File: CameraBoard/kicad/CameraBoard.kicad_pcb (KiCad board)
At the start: 2 copper layers, 101.6 x 76.2 mm, 56 parts, among them Q1 SUD08P06-155L, Q2 SUD08P06-155L, Q3 SUD08P06-155L, U1 LM2678SD-12/NOPB, U1 MP2659GQ-0000-Z

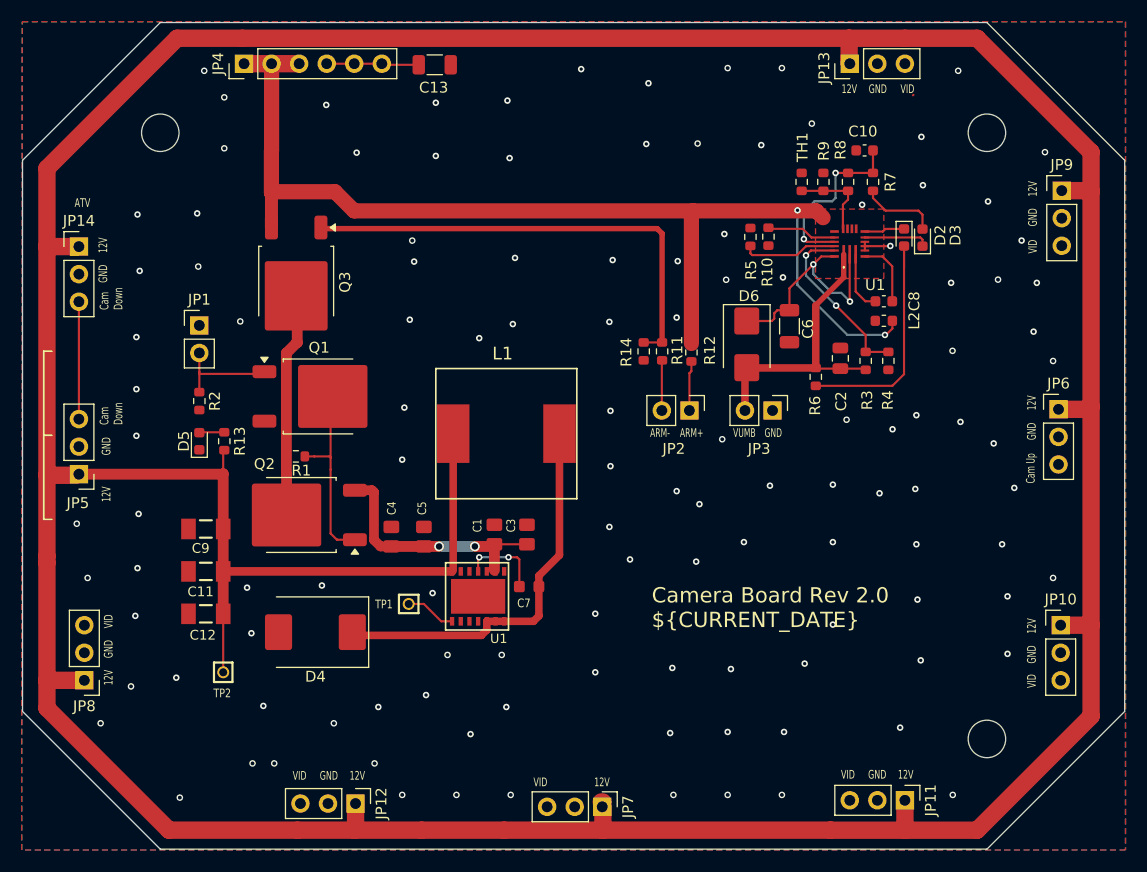
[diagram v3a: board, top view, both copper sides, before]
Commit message: Small update to PCB
Fixed some unsnapped traces
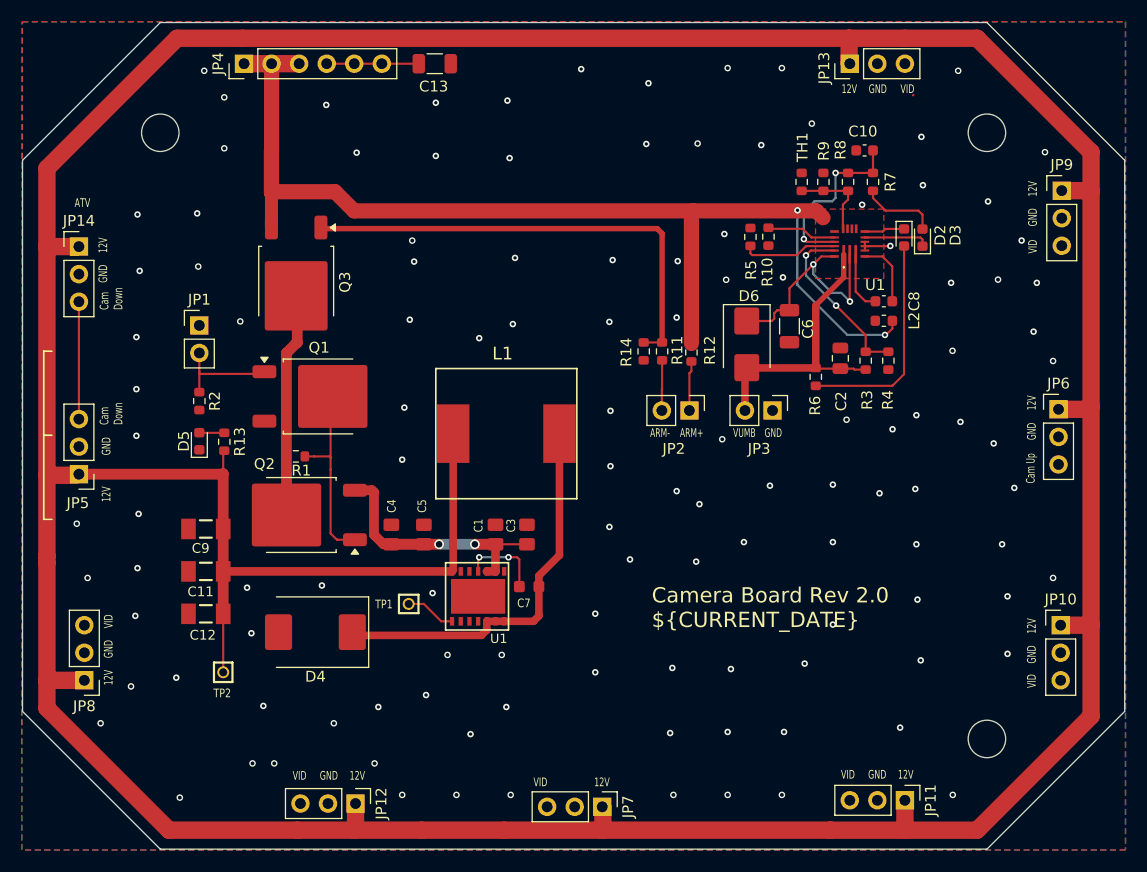
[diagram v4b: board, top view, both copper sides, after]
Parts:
- moved C4 0.20 mm to (131.7, 114.1)
- moved C5 0.20 mm to (134.7, 114.1)
- moved C1 0.10 mm to (141.3, 114.1)
- moved C13 0.10 mm to (135.7, 70.7)
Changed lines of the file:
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@@
 	(footprint "CameraBoard:.0805-B-NOSILK"
 		(layer "F.Cu")
-		(at 141.2 114.1 90)
+		(at 141.3 114.1 90)
 		(descr "0805 (metric 2012) normal 'IPC-B' without silkscreen\nIn house package for nominal spacing based on IPC-7351B. This package is identical to 0805-B, but has its tPlace silkscreen layer removed.")
 		(property "Reference" "C1"
@@
 	(footprint "CameraBoard:.0805-B-NOSILK"
 		(layer "F.Cu")
-		(at 131.7 114.3 90)
+		(at 131.7 114.1 90)
 		(descr "0805 (metric 2012) normal 'IPC-B' without silkscreen\nIn house package for nominal spacing based on IPC-7351B. This package is identical to 0805-B, but has its tPlace silkscreen layer removed.")
 		(property "Reference" "C4"
@@
 	(footprint "CameraBoard:.0805-B-NOSILK"
 		(layer "F.Cu")
-		(at 134.7 114.3 90)
+		(at 134.7 114.1 90)
 		(descr "0805 (metric 2012) normal 'IPC-B' without silkscreen\nIn house package for nominal spacing based on IPC-7351B. This package is identical to 0805-B, but has its tPlace silkscreen layer removed.")
 		(property "Reference" "C5"
@@
 	(footprint "Capacitor_SMD:C_1206_3216Metric"
 		(layer "F.Cu")
-		(at 135.7 70.8)
+		(at 135.7 70.7)
 		(descr "Capacitor SMD 1206 (3216 Metric), square (rectangular) end terminal, IPC-7351 nominal, (Body size source: IPC-SM-782 page 76, https://www.pcb-3d.com/wordpress/wp-content/uploads/ipc-sm-782a_amendment_1_and_2.pdf)")
 		(tags "capacitor")
@@
 	(footprint "Resistor_SMD:R_0603_1608Metric"
 		(layer "F.Cu")
-		(at 116.3 105.5 -90)
+		(at 116.3 105.55 -90)
 		(descr "Resistor SMD 0603 (1608 Metric), square (rectangular) end terminal, IPC-7351 nominal, (Body size source: IPC-SM-782 page 72, https://www.pcb-3d.com/wordpress/wp-content/uploads/ipc-sm-782a_amendment_1_and_2.pdf)")
 		(tags "resistor")
@@
 	(footprint "Resistor_SMD:R_0603_1608Metric"
 		(layer "F.Cu")
-		(at 177.515 98.09375 90)
+		(at 177.515 98.075 90)
 		(descr "Resistor SMD 0603 (1608 Metric), square (rectangular) end terminal, IPC-7351 nominal, (Body size source: IPC-SM-782 page 72, https://www.pcb-3d.com/wordpress/wp-content/uploads/ipc-sm-782a_amendment_1_and_2.pdf)")
 		(tags "resistor")
@@
 	(footprint "Resistor_SMD:R_0603_1608Metric"
 		(layer "F.Cu")
-		(at 175.425 98.09375 -90)
+		(at 175.425 98.075 -90)
 		(descr "Resistor SMD 0603 (1608 Metric), square (rectangular) end terminal, IPC-7351 nominal, (Body size source: IPC-SM-782 page 72, https://www.pcb-3d.com/wordpress/wp-content/uploads/ipc-sm-782a_amendment_1_and_2.pdf)")
 		(tags "resistor")
@@
 	)
 	(gr_line
-		(start 128.325 96.1475)
-		(end 128.325 122.8975)
-		(stroke
-			(width 0.001)
-			(type solid)
-		)
-		(layer "Cmts.User")
-	)
-	(gr_line
 		(start 97.7011 79.6036)
 		(end 97.7011 130.4036)
@@
 	)
 	(segment
-		(start 151.2011 141.3536)
-		(end 151.2011 139.2611)
+		(start 151.2011 139.2611)
+		(end 151.14 139.2)
 		(width 1.6)
 		(layer "F.Cu")
@@
 	)
 	(segment
-		(start 151.2011 138.7536)
-		(end 151.0411 138.7536)
-		(width 1.6)
-		(layer "F.Cu")
-		(net "+12V")
-	)
-	(segment
 		(start 116.2 108.5)
 		(end 116.2 106.425)
@@
 	)
 	(segment
-		(start 102.7 108.64)
-		(end 99.9911 108.64)
+		(start 151.2011 141.3536)
+		(end 151.2011 139.2611)
 		(width 1.6)
 		(layer "F.Cu")
@@
 	)
 	(segment
-		(start 128.3 141.3536)
-		(end 123.0411 141.3536)
+		(start 102.7 108.64)
+		(end 99.9911 108.64)
 		(width 1.6)
 		(layer "F.Cu")
@@
 	)
 	(segment
-		(start 151.2011 139.2611)
-		(end 151.14 139.2)
+		(start 128.3 141.3536)
+		(end 123.0411 141.3536)
 		(width 1.6)
 		(layer "F.Cu")
@@
 		(net "GND")
 	)
-	(segment
-		(start 114.0875 106.2)
-		(end 114 106.2875)
-		(width 0.2)
-		(layer "F.Cu")
-		(net "GND")
-	)
 	(via
 		(at 167.7011 138.1036)
@@
 	)
 	(segment
+		(start 174.4 98.9)
+		(end 175.425 98.9)
+		(width 0.2)
+		(layer "F.Cu")
+		(net "/VUMB")
+	)
+	(segment
 		(start 164.2975 102.66875)
 		(end 164.2975 98.88375)
@@
 	)
 	(segment
-		(start 175.425 98.91875)
-		(end 175.315 98.80875)
+		(start 173.09 98.80875)
+		(end 174.30875 98.80875)
 		(width 0.2)
 		(layer "F.Cu")
@@
 	)
 	(segment
-		(start 175.315 98.80875)
-		(end 173.09 98.80875)
+		(start 174.30875 98.80875)
+		(end 174.4 98.9)
 		(width 0.2)
 		(layer "F.Cu")
@@
 	)
 	(segment
-		(start 141.2 115)
-		(end 141.2 117.4)
-		(width 1)
-		(layer "F.Cu")
-		(net "Net-(Q2-S)")
-	)
-	(segment
-		(start 130.1 114.6)
-		(end 130.1 110.2)
+		(start 130.1 110.2)
+		(end 130.1 114.124999)
 		(width 0.9)
 		(layer "F.Cu")
@@
 	)
 	(segment
-		(start 139.4 115.2)
-		(end 141 115.2)
-		(width 1)
+		(start 141.3 117.5)
+		(end 140.5 117.5)
+		(width 0.8)
 		(layer "F.Cu")
 		(net "Net-(Q2-S)")
 	)
 	(segment
-		(start 140.6 117.4)
-		(end 140.5 117.5)
-		(width 0.2)
+		(start 134.7 115)
+		(end 136.1 115)
+		(width 1)
 		(layer "F.Cu")
 		(net "Net-(Q2-S)")
 	)
 	(segment
-		(start 134.7 115.2)
-		(end 136.1 115.2)
-		(width 1)
+		(start 141.3 115)
+		(end 141.3 117.5)
+		(width 0.8)
 		(layer "F.Cu")
 		(net "Net-(Q2-S)")
 	)
 	(segment
-		(start 131.7 115.2)
-		(end 130.7 115.2)
-		(width 0.9)
+		(start 139.4 115)
+		(end 141.2 115)
+		(width 1)
 		(layer "F.Cu")
 		(net "Net-(Q2-S)")
@@
 	)
 	(segment
-		(start 131.7 115.2)
-		(end 134.7 115.2)
+		(start 131.7 115)
+		(end 134.7 115)
 		(width 1)
 		(layer "F.Cu")
@@
 	)
 	(segment
-		(start 141.2 115)
-		(end 144.2 115)
-		(width 0.2)
+		(start 130.1 114.124999)
+		(end 130.975001 115)
+		(width 0.9)
 		(layer "F.Cu")
 		(net "Net-(Q2-S)")
 	)
 	(segment
-		(start 130.7 115.2)
-		(end 130.1 114.6)
-		(width 0.9)
+		(start 141.2 115)
+		(end 144.2 115)
+		(width 0.2)
 		(layer "F.Cu")
 		(net "Net-(Q2-S)")
 	)
 	(segment
-		(start 141.2 117.4)
-		(end 140.6 117.4)
-		(width 0.2)
+		(start 130.975001 115)
+		(end 131.7 115)
+		(width 0.9)
 		(layer "F.Cu")
 		(net "Net-(Q2-S)")
 	)
 	(via
-		(at 136.1 115.2)
+		(at 136.1 115)
 		(size 0.9)
 		(drill 0.6)
@@
 	)
 	(via
-		(at 139.4 115.2)
+		(at 139.4 115)
 		(size 0.9)
 		(drill 0.6)
@@
 	)
 	(segment
-		(start 136.1 115.2)
-		(end 139.4 115.2)
+		(start 136.1 115)
+		(end 139.4 115)
 		(width 1)
 		(layer "B.Cu")
@@
 	)
 	(segment
-		(start 130.9 70.7)
-		(end 131 70.8)
-		(width 0.2)
-		(layer "F.Cu")
-		(net "Net-(JP4-Pin_4)")
-	)
-	(segment
-		(start 131 70.8)
-		(end 134.225 70.8)
-		(width 0.2)
-		(layer "F.Cu")
-		(net "Net-(JP4-Pin_4)")
-	)
-	(segment
-		(start 128.28 70.7)
-		(end 125.74 70.7)
-		(width 0.2)
-		(layer "F.Cu")
-		(net "Net-(JP4-Pin_4)")
-	)
-	(segment
 		(start 130.82 70.7)
-		(end 130.9 70.7)
+		(end 134.225 70.7)
 		(width 0.2)
 		(layer "F.Cu")
@@
 	)
 	(segment
-		(start 125.575 70.865)
-		(end 125.74 70.7)
+		(start 125.74 70.7)
+		(end 128.28 70.7)
 		(width 0.2)
 		(layer "F.Cu")
@@
 	)
 	(segment
-		(start 116.3 104.675)
-		(end 114.0375 104.675)
+		(start 116.3 104.725)
+		(end 114.0125 104.725)
 		(width 0.2)
 		(layer "F.Cu")
@@
 	)
 	(segment
-		(start 114.0375 104.675)
+		(start 114.0125 104.725)
 		(end 114 104.7125)
 		(width 0.2)
@@
 	)
 	(segment
-		(start 102.9 92.94)
-		(end 102.66 92.7)
-		(width 0.2)
-		(layer "F.Cu")
-		(net "/CAM_DOWN")
-	)
-	(segment
 		(start 102.9 92.64)
 		(end 102.9 103.46)
@@
 	)
 	(segment
-		(start 173.8 83.21875)
-		(end 173.325 83.69375)
+		(start 173.8 82.41875)
+		(end 171.525 82.41875)
 		(width 0.2)
 		(layer "F.Cu")
@@
 	(segment
 		(start 173.8 82.41875)
-		(end 171.525 82.41875)
+		(end 173.8 83.21875)
 		(width 0.2)
 		(layer "F.Cu")
@@
 	)
 	(segment
-		(start 173.325 83.69375)
-		(end 173.325 85.91875)
+		(start 173.8 83.21875)
+		(end 173.325 83.69375)
 		(width 0.2)
 		(layer "F.Cu")
@@
 	)
 	(segment
-		(start 173.8 82.41875)
-		(end 173.8 83.21875)
+		(start 173.325 83.69375)
+		(end 173.325 85.91875)
 		(width 0.2)
 		(layer "F.Cu")
@@
 	)
 	(segment
-		(start 172.55 87.91875)
-		(end 170.375 87.91875)
+		(start 175.425 97.25)
+		(end 175.425 95.725)
 		(width 0.2)
 		(layer "F.Cu")
@@
 	)
 	(segment
-		(start 175.425 95.725)
-		(end 175.425 97.26875)
+		(start 172.55 87.91875)
+		(end 170.375 87.91875)
 		(width 0.2)
 		(layer "F.Cu")
@@
 	)
 	(segment
-		(start 170.375 87.91875)
-		(end 169.925 88.36875)
+		(start 175.425 97.25)
+		(end 177.515 97.25)
 		(width 0.2)
 		(layer "F.Cu")
@@
 	)
 	(segment
-		(start 177.515 97.26875)
-		(end 175.425 97.26875)
+		(start 170.375 87.91875)
+		(end 169.925 88.36875)
 		(width 0.2)
 		(layer "F.Cu")
@@
 	)
 	(segment
-		(start 156.635 98.06875)
-		(end 156.66 98.04375)
+		(start 156.66 98.04375)
+		(end 156.66 100.69)
+		(width 0.2)
+		(layer "F.Cu")
+		(net "/ARM-IN")
+	)
+	(segment
+		(start 156.66 100.69)
+		(end 156.635 100.715)
 		(width 0.2)
 		(layer "F.Cu")
@@
 	)
 	(segment
-		(start 156.635 102.66875)
-		(end 156.635 98.06875)
+		(start 156.635 100.715)
+		(end 156.635 102.66875)
 		(width 0.2)
 		(layer "F.Cu")
